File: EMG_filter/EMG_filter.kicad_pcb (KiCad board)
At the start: 2 copper layers, 43 x 19.5 mm, 16 parts, among them J1 Conn_01x03_Pin, J2 Conn_01x03_Pin, J3 Conn_01x04_Pin, U1 AD620, U2 MCP6022

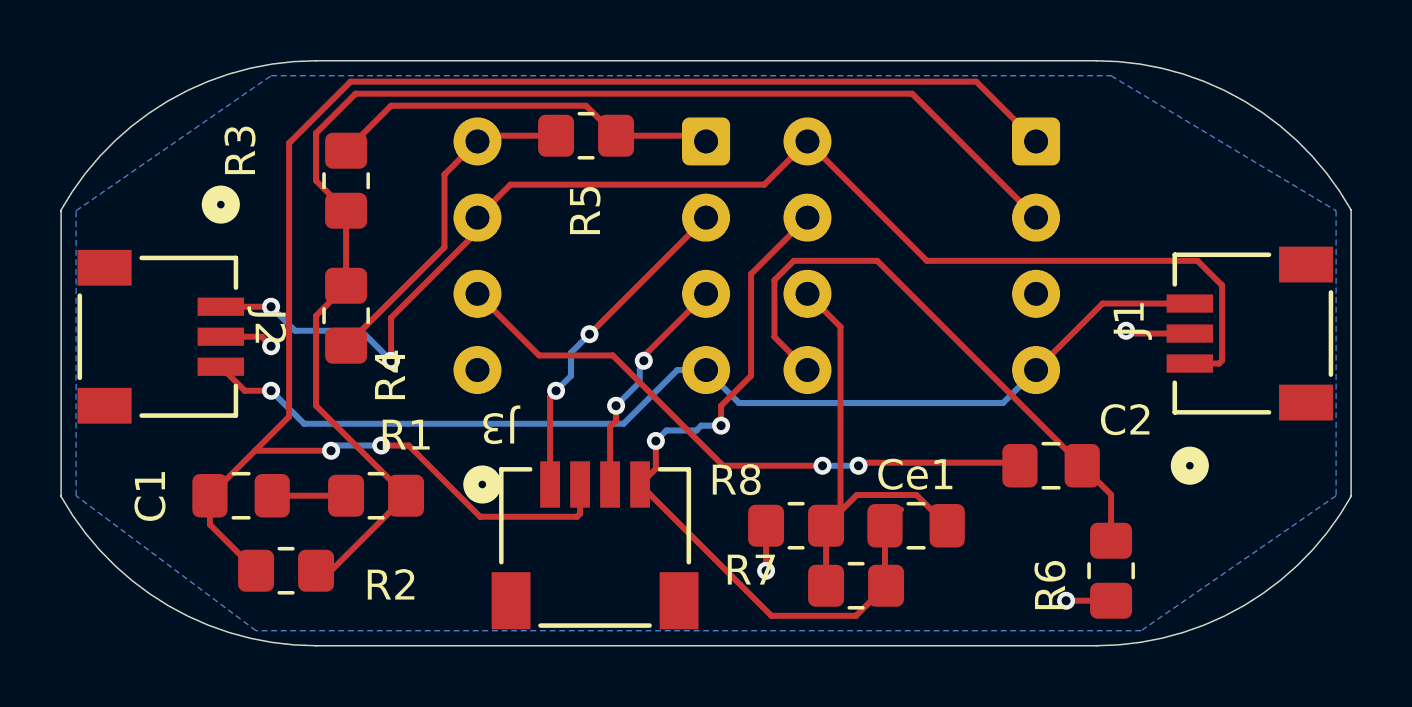
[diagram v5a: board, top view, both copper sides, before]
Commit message: added decoupling caps, bit of rerouting
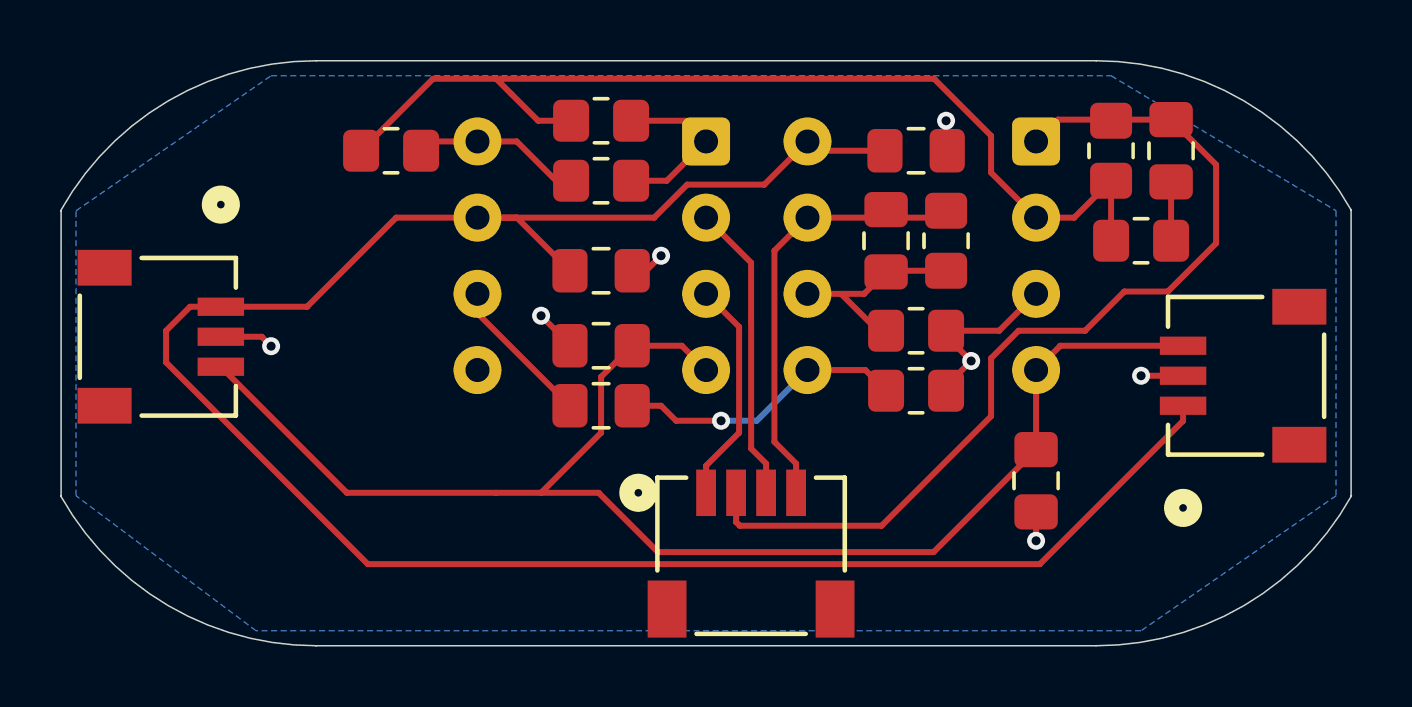
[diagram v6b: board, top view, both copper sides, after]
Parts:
- added C3: C, Capacitor_SMD:C_0805_2012Metric_Pad1.18x1.45mm_HandSolder, F.Cu at (109.0, 109.0)
- added C4: C, Capacitor_SMD:C_0805_2012Metric_Pad1.18x1.45mm_HandSolder, F.Cu at (109.0, 111.5)
- added C5: C, Capacitor_SMD:C_0805_2012Metric_Pad1.18x1.45mm_HandSolder, F.Cu at (119.5, 105.0)
- added C6: C, Capacitor_SMD:C_0805_2012Metric_Pad1.18x1.45mm_HandSolder, F.Cu at (123.5, 116.0)
- moved C1 33.1 mm to (128.0, 105.0), turned to -90 degrees
- moved R2 30.9 mm to (126.0, 105.0), turned to -90 degrees
- moved R1 26.9 mm to (127.0, 108.0), turned to 180 degrees
- moved C2 15.1 mm to (109.0, 113.5)
- moved R7 11.9 mm to (120.5, 108.0), turned to -90 degrees
- moved Ce1 9.55 mm to (118.5, 108.0), turned to -90 degrees
- moved R6 8.85 mm to (119.5, 113.0), turned to 180 degrees
- moved R3 8.73 mm to (109.0, 104.0), turned to 180 degrees
- moved R8 7.63 mm to (119.5, 111.0), turned to 180 degrees
- moved R4 5.70 mm to (102.0, 105.0), turned to 0 degrees
- moved J3 5.21 mm to (114.0, 118.5)
- moved R5 1.58 mm to (109.0, 106.0)
- moved J1 1.42 mm to (130.5, 112.5)
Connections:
- J3 pad 1: -In -> +In
- J3 pad 3: +In -> -In
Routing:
- net +5V: track 43.9 -> 71.2 mm, vias 2 -> 0
- net PATIENT_GND: track 55.5 -> 31.6 mm, vias 2 -> 0
- net Net-(C2-Pad1): track 21.3 -> 5.72 mm, vias 2 -> 0
- net GND: track 35.7 -> 48.0 mm, vias 1 -> 0
- net Net-(U2A--): track 44.5 -> 34.2 mm
- net Net-(U2B-+): track 19.7 -> 9.66 mm, vias 0 -> 1
- net Output: track 25.4 -> 15.4 mm, vias 2 -> 0
- net Net-(U2B--): track 15.3 -> 7.68 mm
- net Net-(R3-Pad1): track 13.1 -> 5.83 mm
- net +2V5: track 6.97 -> 14.0 mm, vias 4 -> 7
- net Net-(R4-Pad2): track 11.3 -> 6.69 mm
- net -In: track 11.0 -> 10.00 mm, vias 2 -> 0
- net Net-(C1-Pad2): track 2.46 -> 1.96 mm
- net +In: track 7.68 -> 8.04 mm, vias 2 -> 0

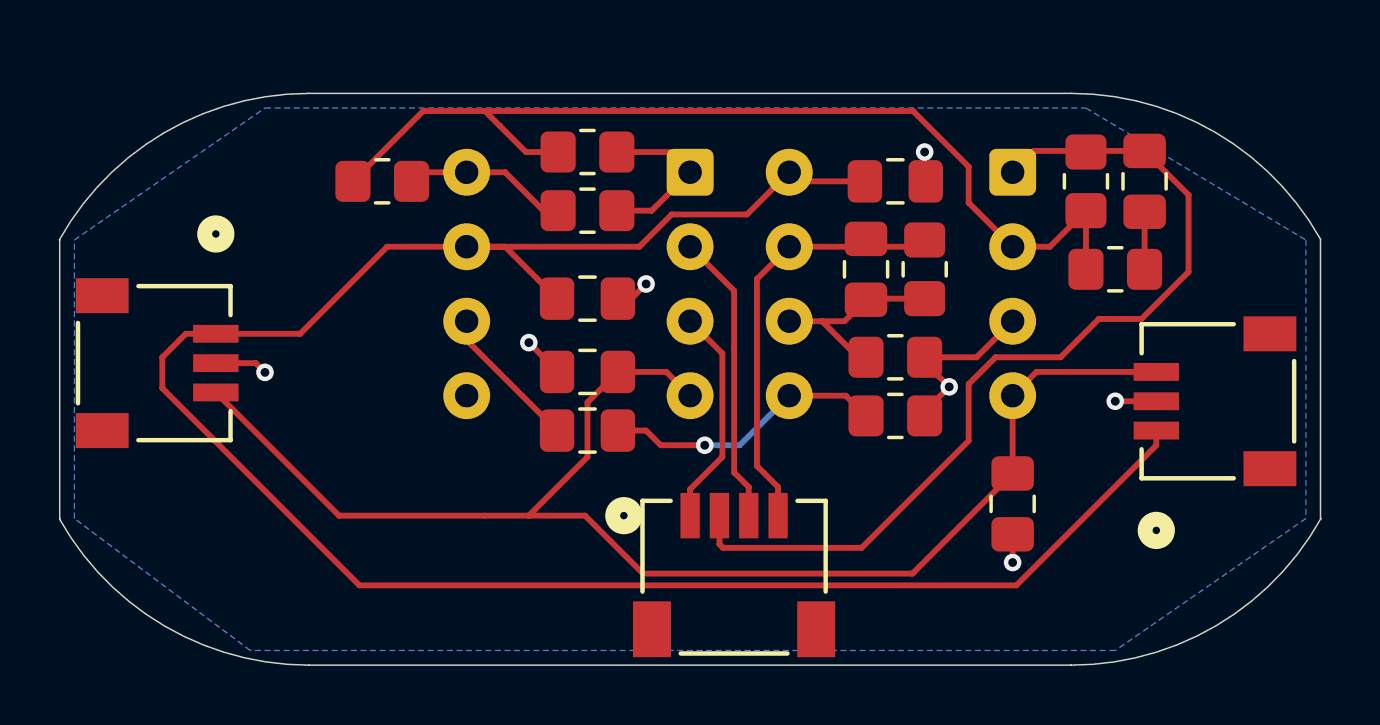
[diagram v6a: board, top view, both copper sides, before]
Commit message: added mounting holes
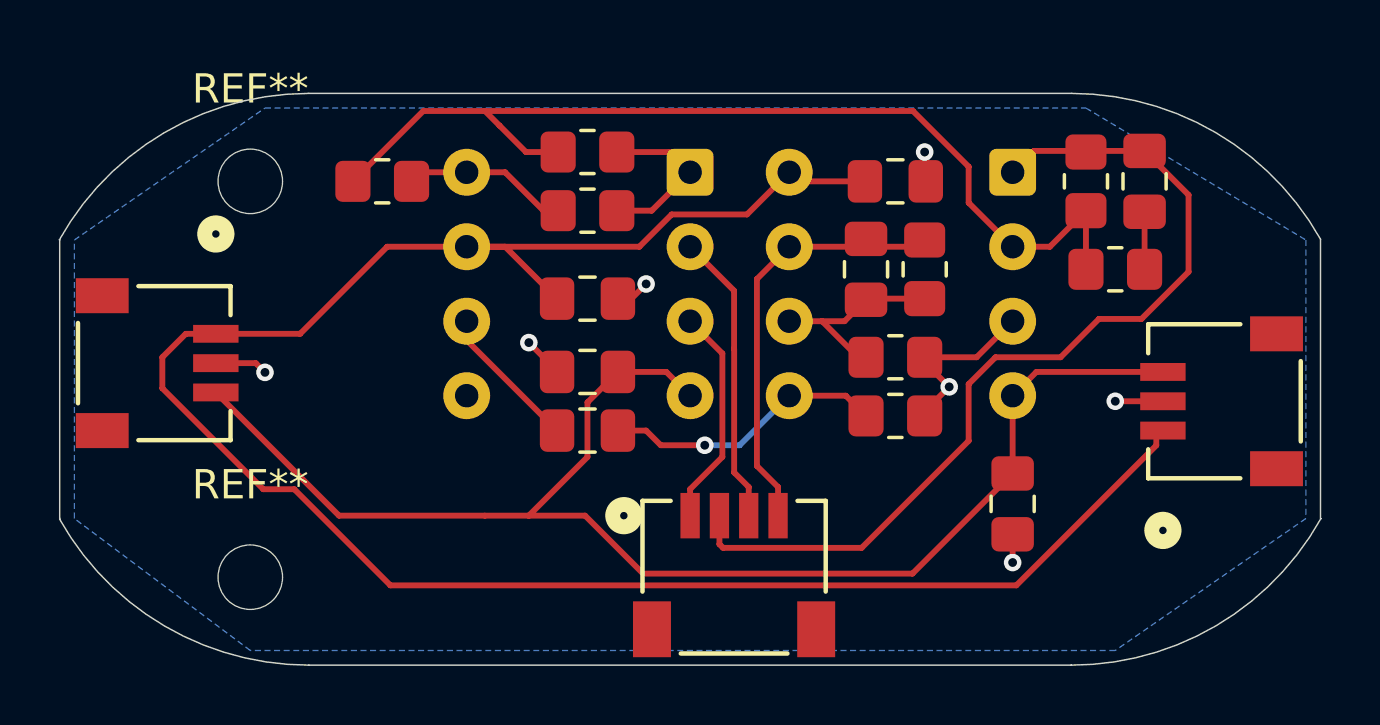
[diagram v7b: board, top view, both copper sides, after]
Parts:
- added REF**: MountingHole_2.2mm_M2, MountingHole:MountingHole_2.2mm_M2, F.Cu at (97.5, 105.0)
- added REF**: MountingHole_2.2mm_M2, MountingHole:MountingHole_2.2mm_M2, F.Cu at (97.5, 118.5)
- moved J1 0.22 mm to (130.7, 112.5)
